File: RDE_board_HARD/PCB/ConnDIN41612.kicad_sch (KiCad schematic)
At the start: 34 parts, among them IC1 SN65HVD75DR, J1 DIN41612_02x32_AC, T1 H1102NL, U3 USBLC6-2SC6, U4 USBLC6-2SC6, U5 USBLC6-2SC6

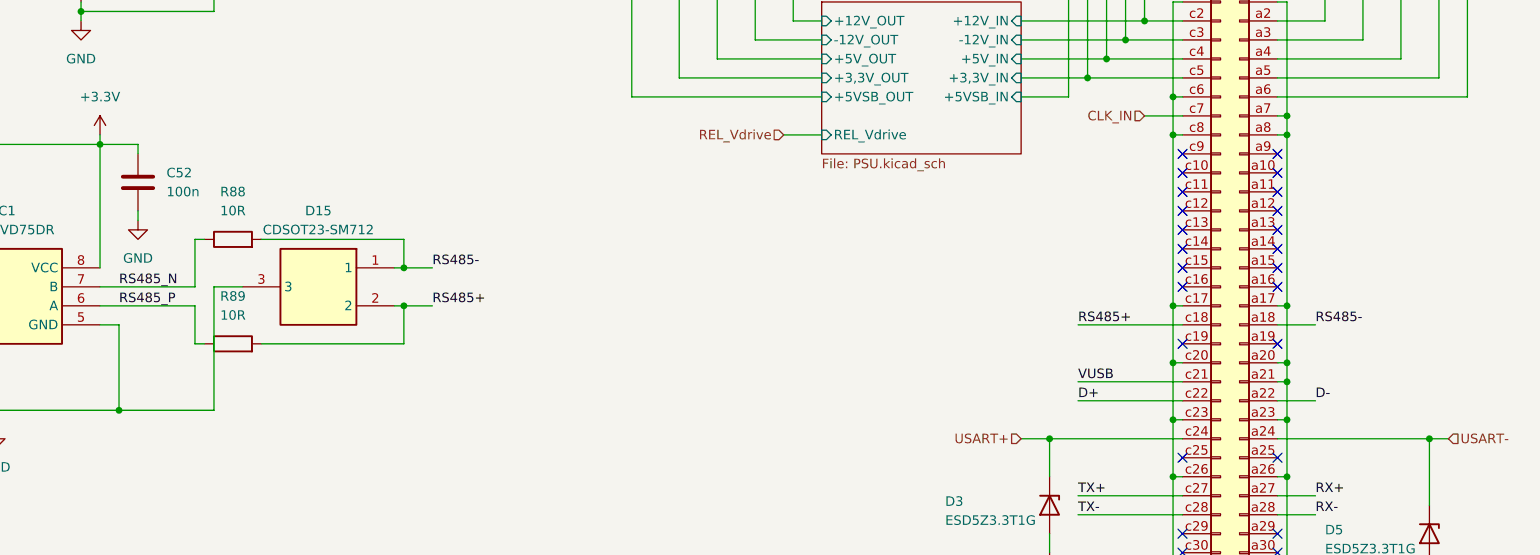
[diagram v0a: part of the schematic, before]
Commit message: Added i2c for backplane config, testpoints. File organization
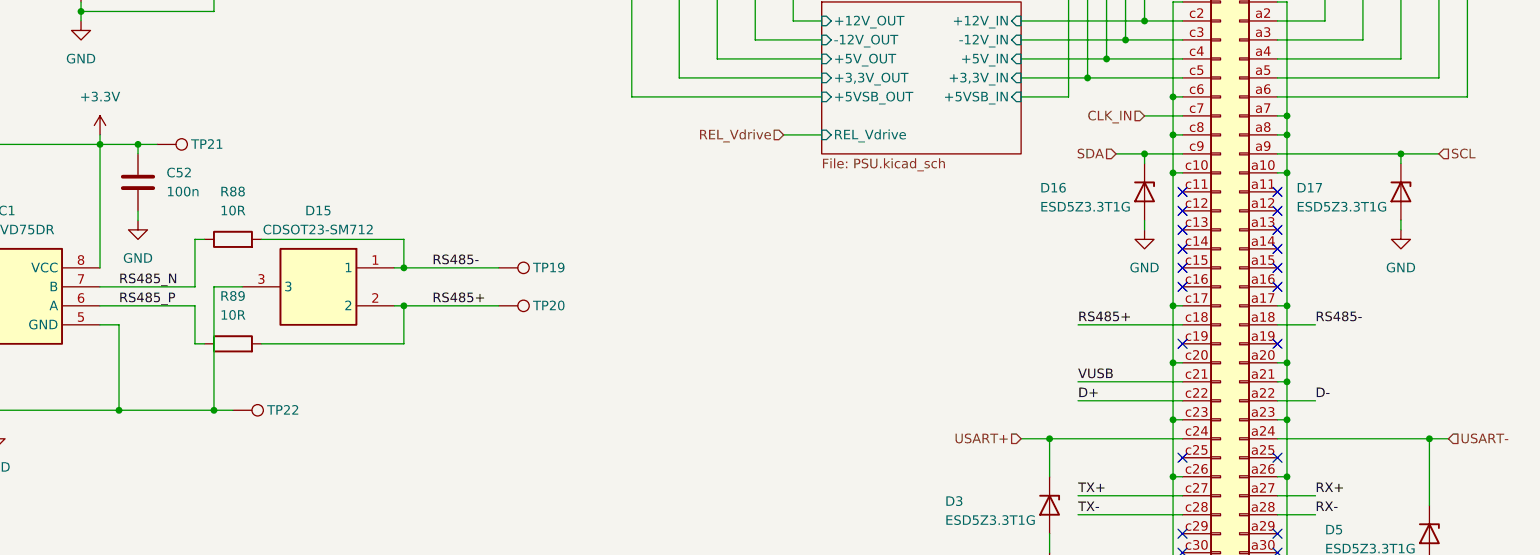
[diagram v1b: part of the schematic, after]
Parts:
- added D16, D17: ESD5Z3.3T1G, Diode_SMD:D_SOD-523, symbol Diode:ESD5Zxx
- added TP19, TP20, TP21, TP22: TestPoint, TestPoint:TestPoint_Pad_D1.0mm, symbol Connector:TestPoint
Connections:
- net +3.3V: now also TP21.1
- net GND: now also J1.a10 (Pin_a10), J1.c10 (Pin_c10), D16.2 (A), D17.2 (A), TP22.1
- net RS485+: now also TP20.1
- net RS485-: now also TP19.1
- net SCL: now reaches J1.a9 (Pin_a9)
- net SCL: now also D17.1 (K)
- net SDA: now reaches J1.c9 (Pin_c9)
- net SDA: now also D16.1 (K)
- no-connect marks 28 -> 24
